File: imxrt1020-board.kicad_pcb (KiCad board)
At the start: 2 copper layers, 102.9 x 68.6 mm, 168 parts, among them J1 Micro_SD_Card_Det, J10 CASTELATED, J11 CASTELATED, J12 CASTELATED, J13 CASTELATED, J14 CASTELATED, J15 CASTELATED, J16 CASTELATED, J17 CASTELATED, J18 CASTELATED, J19 CASTELATED, J2 USB_OTG, J20 CASTELATED, J21 CASTELATED, J22 CASTELATED, J23 CASTELATED, J24 CASTELATED, J25 CASTELATED, J26 CASTELATED, J27 CASTELATED, J28 CASTELATED, J29 CASTELATED, J3 Conn_02x20_Odd_Even, J30 CASTELATED, J31 CASTELATED, J32 CASTELATED, J33 CASTELATED, J34 CASTELATED, J35 CASTELATED, J36 CASTELATED, J37 CASTELATED, J38 CASTELATED, J39 CASTELATED, J4 CASTELATED, J40 CASTELATED, J41 CASTELATED, J42 CASTELATED, J43 CASTELATED, J44 GS2, J45 GS2, J46 PWR_IN, J47 JTAG, J48 Conn_01x05, J49 CASTELATED, J5 CASTELATED, J50 CASTELATED, J51 CASTELATED, J52 CASTELATED, J53 CASTELATED, J54 CASTELATED, J55 CASTELATED, J56 CASTELATED, J57 CASTELATED, J58 RJ45-TRANSFO, J59 CASTELATED, J6 CASTELATED, J60 CASTELATED, J61 CASTELATED, J62 CASTELATED, J63 CASTELATED, J64 CASTELATED, J65 CASTELATED, J66 CASTELATED, J7 CASTELATED, J8 CASTELATED, J9 CASTELATED, SW1 RST, SW2 SW_DIP_x02, U1 imx_rt1020-qfp144, U2 M25PX32-VMW, U3 AS4C16M16S, U4 TPS3839DBZ, U5 NCP1117-3.3_SOT223, U6 ISL3178E, U7 KSZ8081RNA, U8 TCAN332D, Y1 24MHz, Y2 32.768Khz

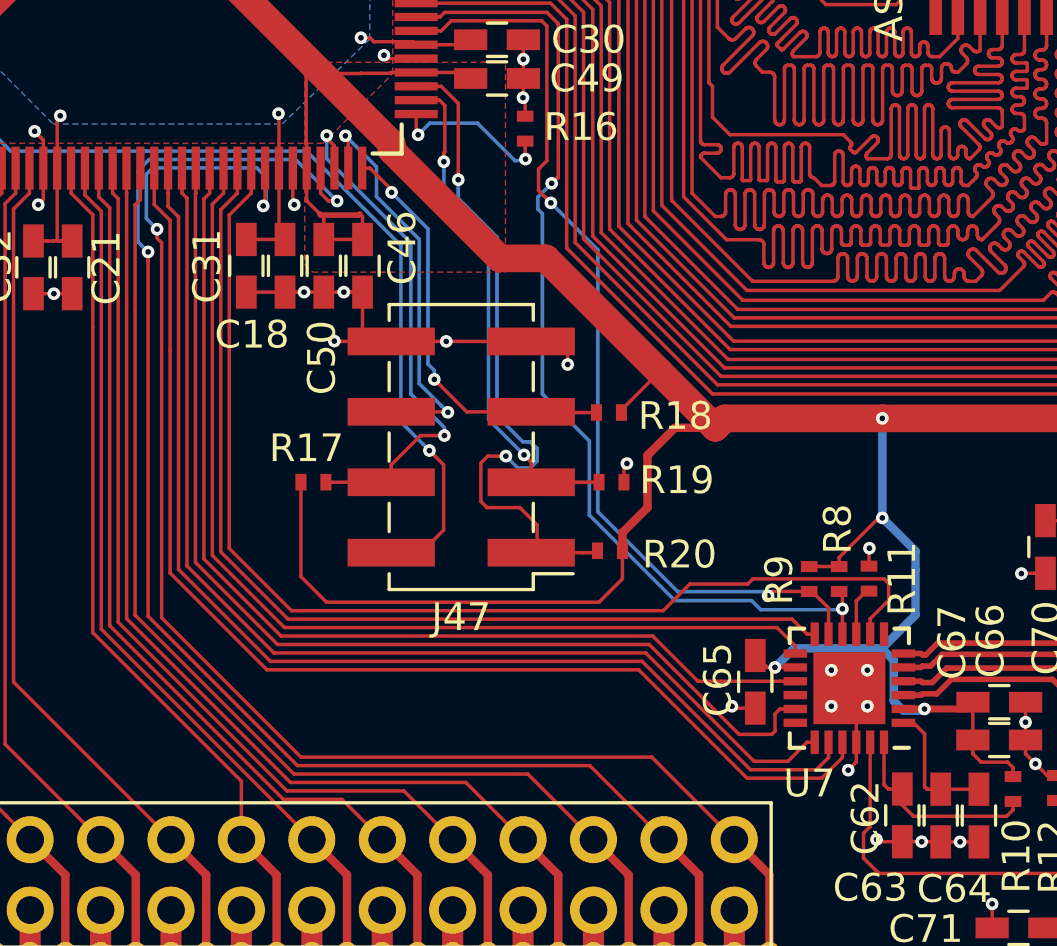
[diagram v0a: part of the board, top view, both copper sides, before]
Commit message: Tune length of ethernet MAC to PHY lines
Signed-off-by: Martin Ribelotta <martinribelotta@gmail.com>
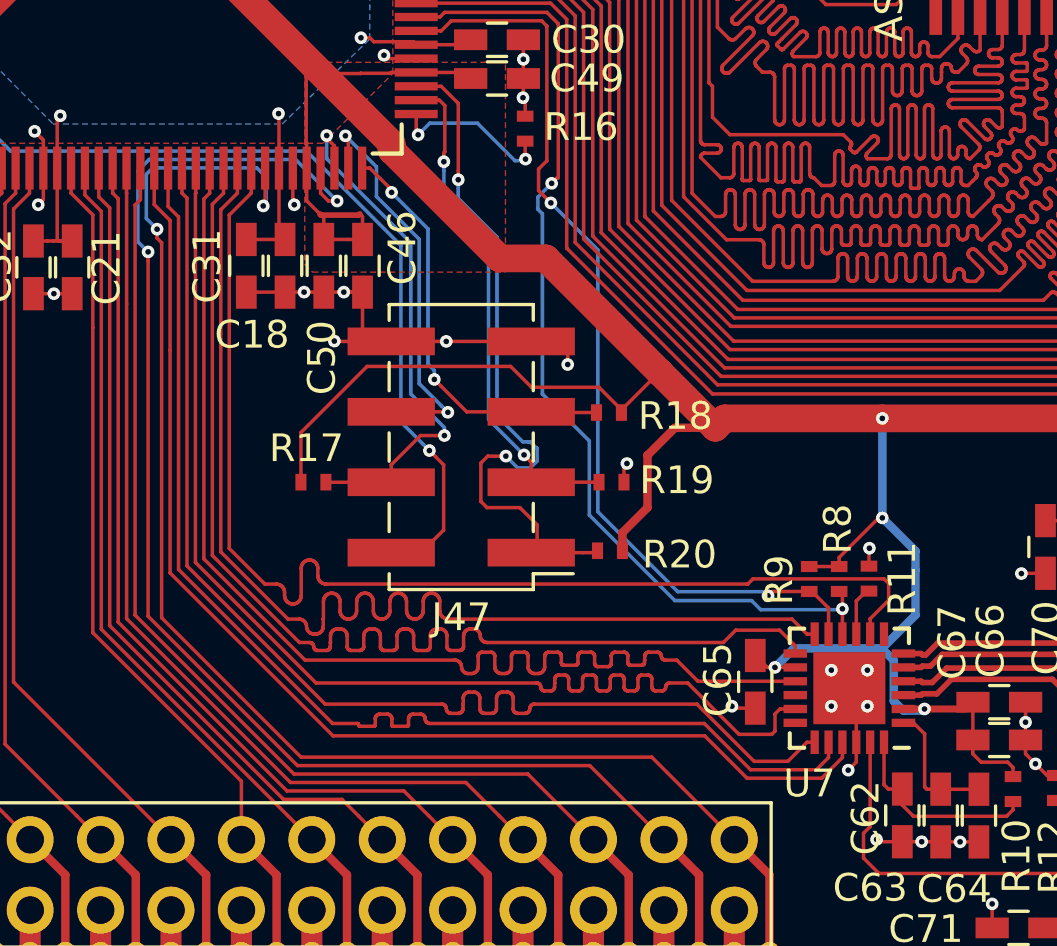
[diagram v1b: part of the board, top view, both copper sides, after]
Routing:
- net /GPIO/ENET_RXD1: track 36.7 -> 43.0 mm
- net /GPIO/ENET_RXD0: track 36.8 -> 43.1 mm
- net /GPIO/ENET_CRS_DV: track 37.3 -> 43.1 mm
- net /GPIO/ENET_RX_ER: track 39.2 -> 43.1 mm
- net /GPIO/ENET_TX_EN: track 40.3 -> 43.1 mm
- net +3V3: track 550.1 -> 548.4 mm
- net /GPIO/ENET_TX_CLK: track 41.4 -> 43.0 mm
- net /GPIO/ENET_TXD0: track 41.8 -> 43.1 mm

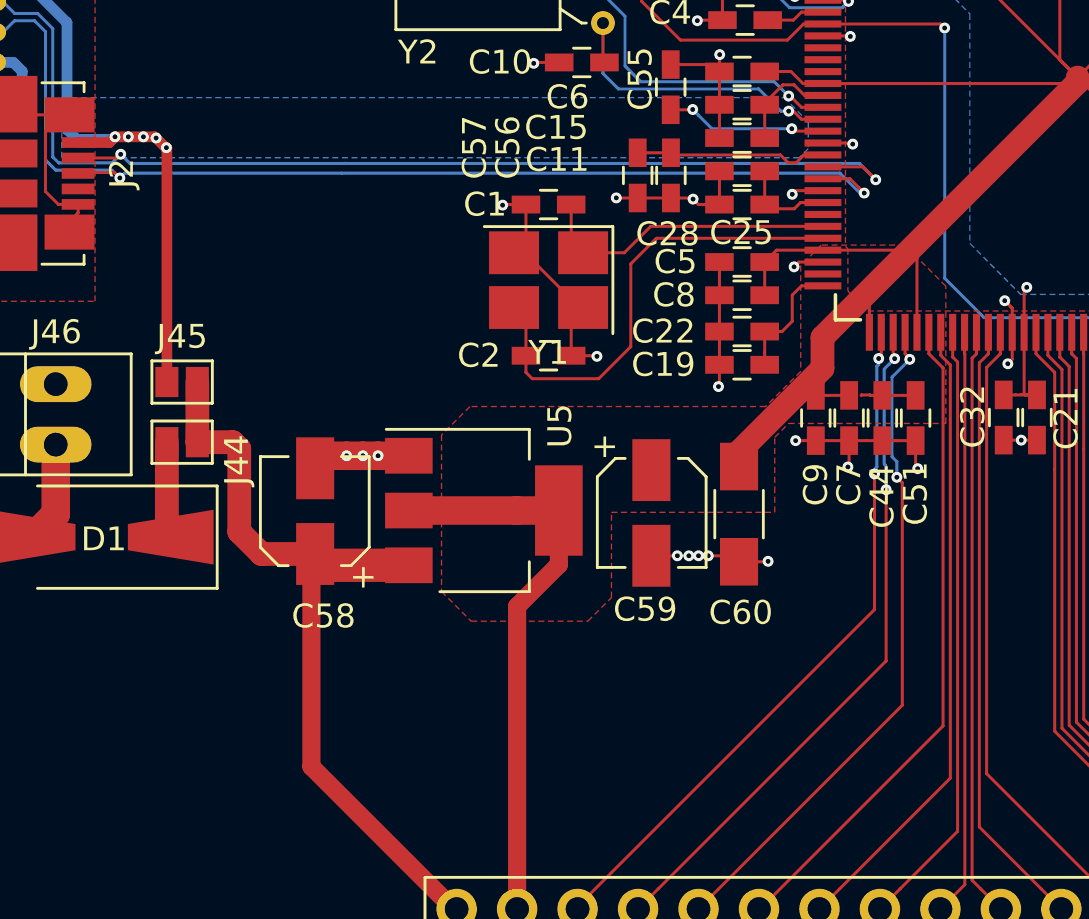
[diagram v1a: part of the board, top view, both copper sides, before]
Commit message: Change 3v3@1A regulator by AZ1084-3.3@5A
Signed-off-by: Martin Ribelotta <martinribelotta@gmail.com>
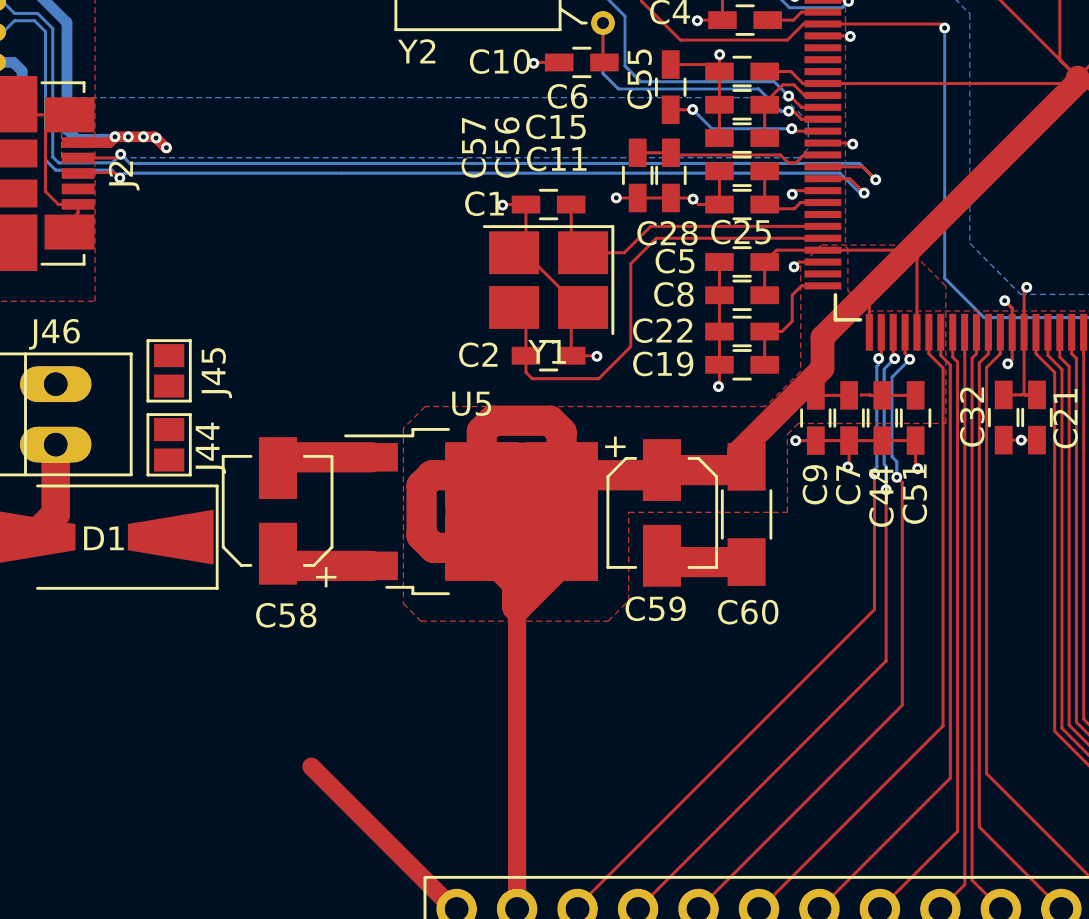
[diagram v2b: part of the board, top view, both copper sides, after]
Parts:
- U5: value NCP1117-3.3_SOT223 -> LM1084-3.3; footprint TO_SOT_Packages_SMD:SOT-223-3_TabPin2 -> TO_SOT_Packages_SMD:TO-252-2
- moved C58 1.56 mm to (120.6, 118.0)
- moved J45 0.72 mm to (116.0, 112.1), turned to 180 degrees
- moved J44 0.56 mm to (116.0, 115.2), turned to 0 degrees
- moved U5 0.51 mm to (128.7, 118.1)
- moved C59 0.44 mm to (136.7, 118.1)
- moved C60 0.32 mm to (140.3, 118.2)
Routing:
- net +5V: track 41.8 -> 17.8 mm
- net +3V3: track 548.4 -> 566.5 mm
- net /POWER/PWR_IN1: track 32.2 -> 22.4 mm
- net /GPIO/DC_IN: track 4.05 -> 0.23 mm
- net GND: track 275.6 -> 274.2 mm, vias 98 -> 90

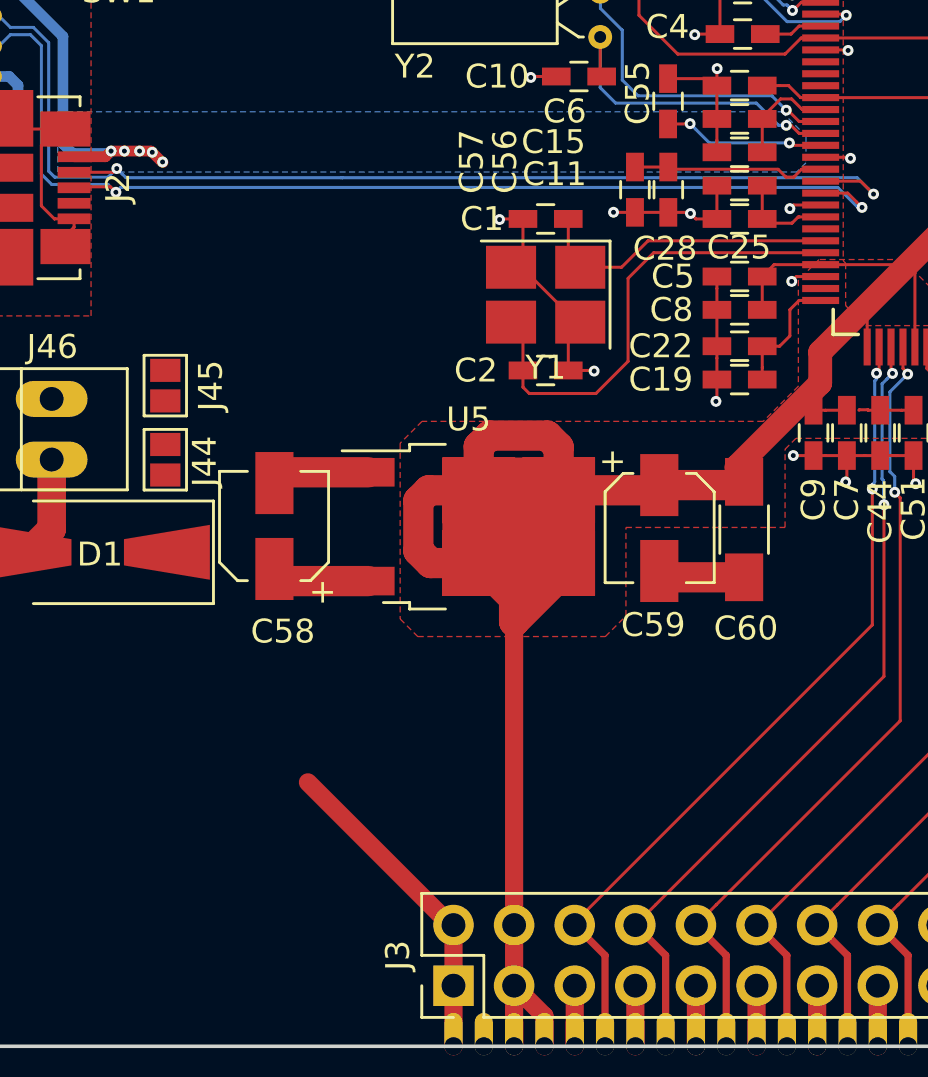
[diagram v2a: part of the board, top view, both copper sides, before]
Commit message: Fix gnd of regulator Signed-off-by: Martin Ribelotta <martinribelotta@gmail.com>
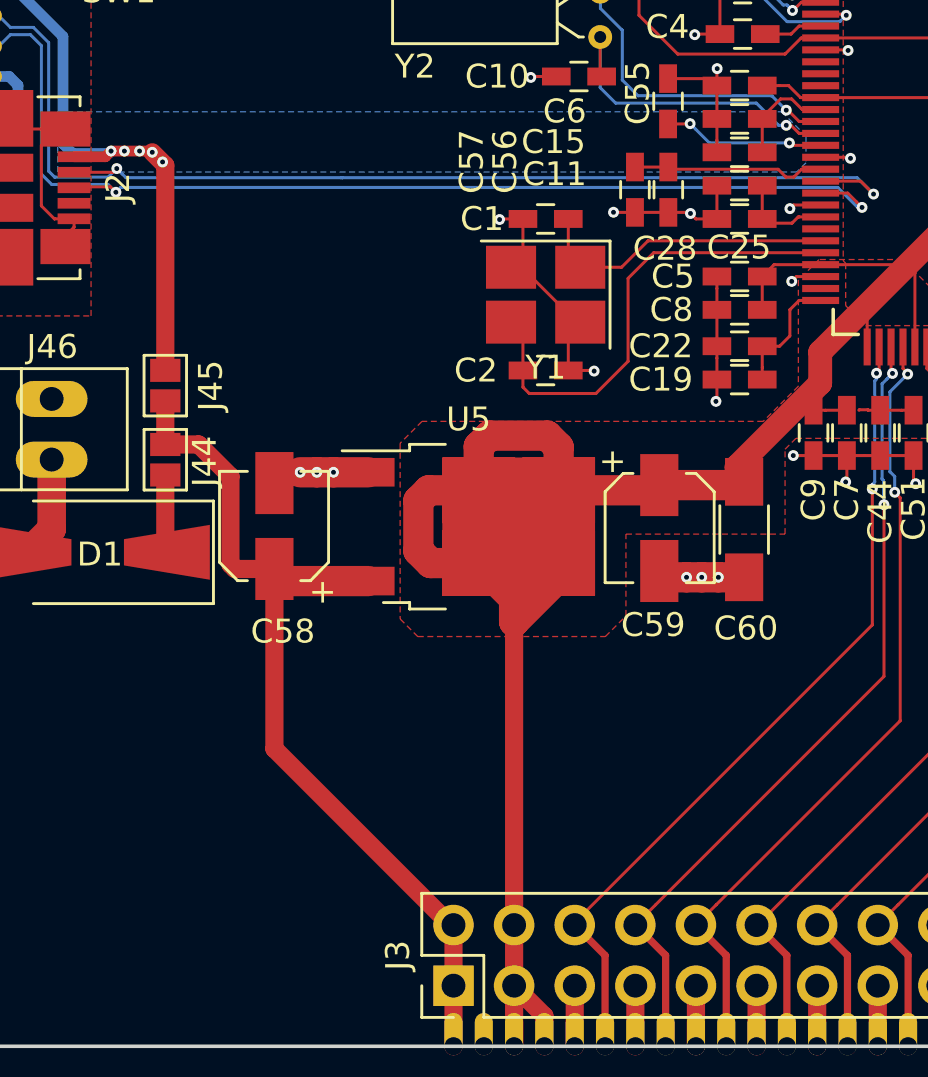
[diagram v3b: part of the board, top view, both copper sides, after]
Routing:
- net +5V: track 17.8 -> 38.1 mm
- net /POWER/PWR_IN1: track 22.4 -> 31.7 mm
- net /GPIO/DC_IN: track 0.23 -> 3.50 mm
- net GND: vias 90 -> 96
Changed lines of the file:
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@@
     (thickness 1.6)
     (drawings 6)
-    (tracks 15155)
+    (tracks 15178)
     (zones 0)
     (modules 168)
@@
   (segment (start 135.135 107.181) (end 133.403 107.181) (width 0.127) (layer F.Cu) (net 7))
   (segment (start 143.478 106.072) (end 136.244 106.072) (width 0.127) (layer F.Cu) (net 7))
-  (segment (start 124.5235 115.7725) (end 121.0385 115.7725) (width 1.27) (layer F.Cu) (net 8))
+  (segment (start 122.3645 115.7725) (end 121.666 115.7725) (width 1.27) (layer F.Cu) (net 8))
+  (segment (start 123.063 115.7725) (end 122.3645 115.7725) (width 1.27) (layer F.Cu) (net 8))
+  (via (at 122.3645 115.7725) (size 0.4572) (drill 0.2032) (layers F.Cu B.Cu) (net 8))
+  (segment (start 121.0385 115.7725) (end 121.666 115.7725) (width 0.127) (layer F.Cu) (net 8))
+  (via (at 121.666 115.7725) (size 0.4572) (drill 0.2032) (layers F.Cu B.Cu) (net 8))
+  (segment (start 124.5235 115.7725) (end 123.063 115.7725) (width 1.27) (layer F.Cu) (net 8))
+  (via (at 123.063 115.7725) (size 0.4572) (drill 0.2032) (layers F.Cu B.Cu) (net 8))
+  (segment (start 138.4935 120.1735) (end 137.8585 120.1735) (width 1.27) (layer F.Cu) (net 8))
+  (segment (start 139.192 120.1735) (end 138.4935 120.1735) (width 1.27) (layer F.Cu) (net 8))
+  (via (at 138.4935 120.1735) (size 0.4572) (drill 0.2032) (layers F.Cu B.Cu) (net 8))
+  (segment (start 140.2715 120.1735) (end 139.192 120.1735) (width 1.27) (layer F.Cu) (net 8))
+  (via (at 139.192 120.1735) (size 0.4572) (drill 0.2032) (layers F.Cu B.Cu) (net 8))
+  (segment (start 137.8585 120.1735) (end 136.979 120.1735) (width 1.27) (layer F.Cu) (net 8))
+  (via (at 137.8585 120.1735) (size 0.4572) (drill 0.2032) (layers F.Cu B.Cu) (net 8))
   (segment (start 121.0385 115.7725) (end 120.5865 116.2245) (width 1.27) (layer F.Cu) (net 8))
-  (segment (start 140.2715 120.1735) (end 136.979 120.1735) (width 1.27) (layer F.Cu) (net 8))
   (segment (start 136.979 120.1735) (end 136.7155 119.91) (width 1.27) (layer F.Cu) (net 8))
   (segment (start 181.21122 124.88122) (end 181.21122 124.24918) (width 0.127) (layer F.Cu) (net 8))
@@
   (segment (start 142.576 105.072) (end 143.478 105.072) (width 0.127) (layer F.Cu) (net 18))
   (segment (start 141.031 105.156) (end 141.031 103.759) (width 0.127) (layer F.Cu) (net 18))
+  (segment (start 118.745 119.634) (end 118.9355 119.8245) (width 0.762) (layer F.Cu) (net 19))
+  (segment (start 118.9355 119.8245) (end 120.5865 119.8245) (width 0.762) (layer F.Cu) (net 19))
+  (segment (start 118.745 115.941) (end 118.745 119.634) (width 0.762) (layer F.Cu) (net 19))
+  (segment (start 116.0145 114.6075) (end 117.4115 114.6075) (width 0.762) (layer F.Cu) (net 19))
+  (segment (start 117.4115 114.6075) (end 118.745 115.941) (width 0.762) (layer F.Cu) (net 19))
+  (segment (start 116.0145 114.6075) (end 116.0145 112.781) (width 0.762) (layer F.Cu) (net 19))
+  (segment (start 128.0922 134.747) (end 127.97282 134.747) (width 0.762) (layer F.Cu) (net 19))
+  (segment (start 127.97282 134.747) (end 120.5865 127.36068) (width 0.762) (layer F.Cu) (net 19))
+  (segment (start 120.5865 127.36068) (end 120.5865 119.8245) (width 0.762) (layer F.Cu) (net 19))
   (segment (start 124.5235 120.3325) (end 121.0945 120.3325) (width 1.27) (layer F.Cu) (net 19))
   (segment (start 121.0945 120.3325) (end 120.5865 119.8245) (width 1.27) (layer F.Cu) (net 19))
-  (segment (start 121.99112 128.7653) (end 127.97282 134.747) (width 0.762) (layer F.Cu) (net 19))
-  (segment (start 127.97282 134.747) (end 128.0922 134.747) (width 0.762) (layer F.Cu) (net 19))
   (segment (start 128.0922 137.287) (end 128.0922 134.747) (width 0.762) (layer F.Cu) (net 19))
   (segment (start 128.0922 139.827) (end 128.0922 137.287) (width 0.762) (layer F.Cu) (net 19))
@@
   (segment (start 168.8084 110.1852) (end 168.8211 110.1979) (width 0.127) (layer F.Cu) (net 75))
   (via (at 168.8211 110.1979) (size 0.4572) (drill 0.2032) (layers F.Cu B.Cu) (net 75))
+  (segment (start 116.0145 115.8875) (end 116.0145 119.0581) (width 0.762) (layer F.Cu) (net 76))
+  (segment (start 116.0145 119.0581) (end 116.0824 119.126) (width 0.762) (layer F.Cu) (net 76))
   (segment (start 115.9206 118.9642) (end 116.0824 119.126) (width 1) (layer F.Cu) (net 76))
   (segment (start 111.252 115.2398) (end 111.252 118.1564) (width 1.2) (layer F.Cu) (net 77))
   (segment (start 111.252 118.1564) (end 110.2824 119.126) (width 1.2) (layer F.Cu) (net 77))
+  (segment (start 116.0145 111.501) (end 116.0145 102.9081) (width 0.762) (layer F.Cu) (net 78))
+  (segment (start 116.0145 102.9081) (end 115.4684 102.362) (width 0.762) (layer F.Cu) (net 78))
   (segment (start 107.7722 95.377) (end 109.59084 95.377) (width 0.45) (layer B.Cu) (net 78))
   (segment (start 109.59084 95.377) (end 111.72444 97.5106) (width 0.45) (layer B.Cu) (net 78))
@@
         (xy 142.4432 114.3508) (xy 148.6408 114.3508) (xy 148.6408 108.585) (xy 146.9136 106.8578) (xy 143.4084 106.8578)
         (xy 142.5448 107.7214) (xy 142.5448 112.1664) (xy 141.0716 113.6396) (xy 126.7714 113.6396) (xy 125.857 114.554)
-        (xy 125.857 121.92) (xy 126.5936 122.6566) (xy 134.4549 122.6566) (xy 135.3185 121.793) (xy 135.3185 118.0846)
-        (xy 141.986 118.0846) (xy 141.986 114.808)
+        (xy 125.857 121.92) (xy 126.5936 122.6566) (xy 134.4549 122.6566) (xy 135.3185 121.793) (xy 135.3185 118.364)
+        (xy 141.986 118.364) (xy 141.986 114.808)
       )
     )
